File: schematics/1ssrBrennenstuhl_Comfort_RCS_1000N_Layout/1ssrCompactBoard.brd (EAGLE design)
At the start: 46 x 47 mm, 20 parts, among them K1 AQG12105

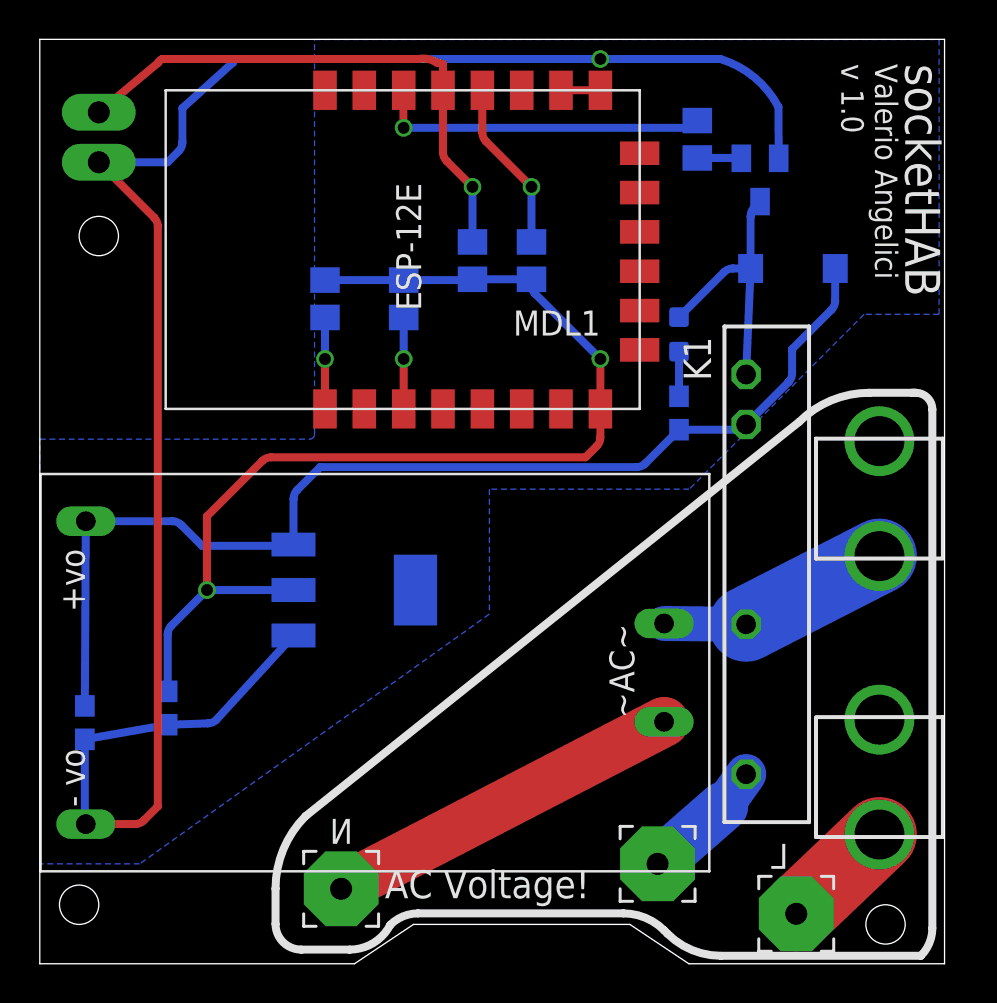
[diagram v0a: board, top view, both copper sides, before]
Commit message: diode moved
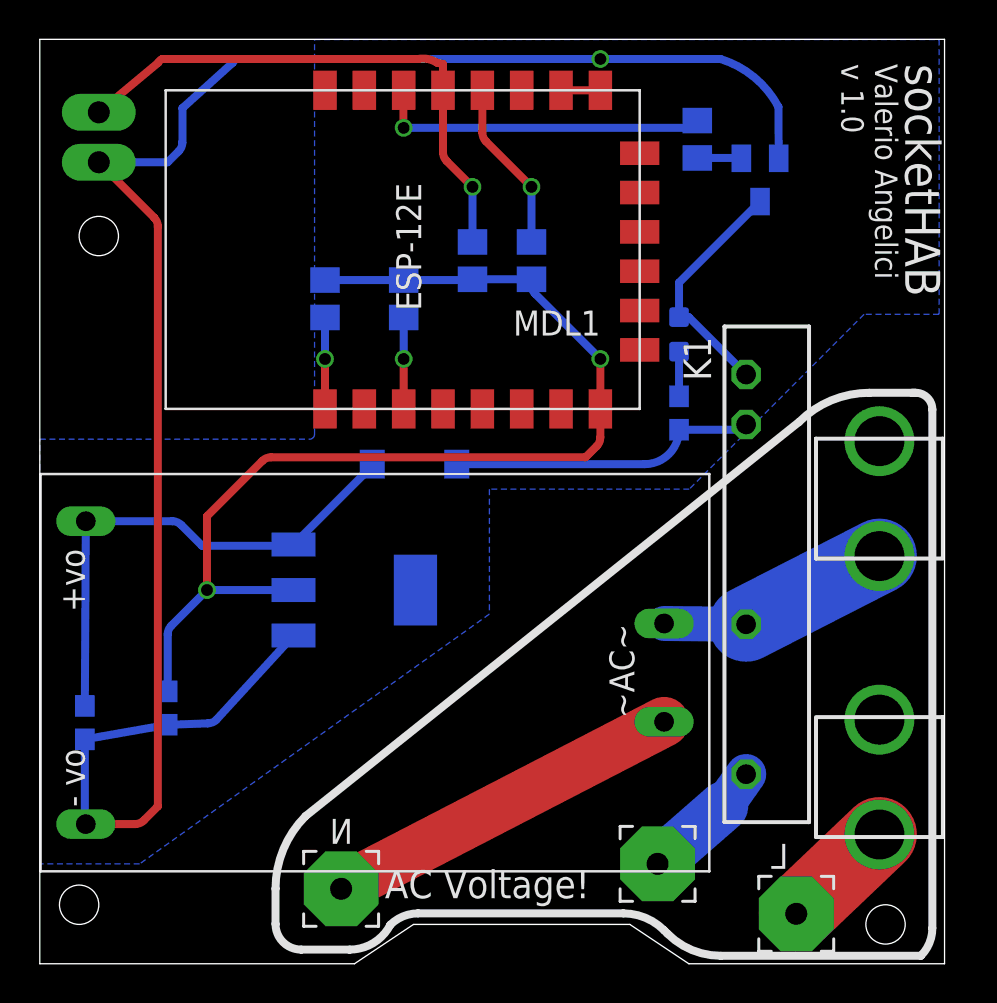
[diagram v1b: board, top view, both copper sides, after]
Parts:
- removed D1: (no value), SparkFun-DiscreteSemi:SMA-DIODE
- added D3: (no value), SparkFun-DiscreteSemi:SMA-DIODE
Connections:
- new net N$3: D3.C, K1.+, R4.2
- net 5V: now also D3.A; no longer D1.C, K1.+, R4.2
- net N$10: no longer D1.A
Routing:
- net 5V: track 57.1 -> 26.3 mm
- net N$3: track 0.00 -> 15.7 mm
- net N$10: track 13.6 -> 12.2 mm
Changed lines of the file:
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@@
 <setting verticaltext="up"/>
 </settings>
-<grid distance="0.05" unitdist="inch" unit="inch" style="lines" multiple="1" display="yes" altdistance="0.025" altunitdist="inch" altunit="inch"/>
+<grid distance="0.05" unitdist="inch" unit="mm" style="lines" multiple="1" display="yes" altdistance="0.025" altunitdist="inch" altunit="mm"/>
 <layers>
 <layer number="1" name="Top" color="4" fill="1" visible="yes" active="yes"/>
@@
 <text x="40.75" y="45.75" size="1.143" layer="112" rot="SR270">Valerio Angelici
 v 1.0</text>
-<text x="6.25" y="8" size="1.016" layer="122" distance="56" rot="MR180">https://github.com/valerioangelici/socketHAB</text>
+<text x="4.98" y="44.83" size="1.016" layer="122" distance="56" rot="MR180">https://github.com/valerioangelici/socketHAB</text>
 <text x="40.75" y="30.5" size="1.143" layer="122" rot="SMR90">Valerio Angelici
 v 1.0</text>
-<text x="23.25" y="9.75" size="1.016" layer="122" rot="SMR0">Fits a Brennstuhl
+<text x="19.44" y="37.69" size="1.016" layer="122" rot="SMR0">Fits a Brennstuhl
 Comfort RCS 1000N</text>
 <wire x1="44.483065625" y1="29.02995" x2="42.183034375" y2="29.02995" width="0.4064" layer="112"/>
@@
 <attribute name="PROD_ID" value="CAP-08604" x="6.5" y="13" size="1.778" layer="28" rot="MR270" display="off"/>
 </element>
-<element name="D1" library="SparkFun-DiscreteSemi" package="SMA-DIODE" value="" x="38.29" y="35.35" rot="MR180"/>
 <element name="K1" library="relay" package="AQG" value="AQG12105" x="35.91" y="19.8" rot="R270">
 <attribute name="MF" value="AROMAT/ MATSUSHITA" x="35.91" y="19.8" size="1.778" layer="27" rot="R270" display="off"/>
@@
 </element>
 <element name="J1" library="SparkFun-Connectors" package="1X02_LONGPADS" value="" x="3" y="40.75" rot="R90"/>
+<element name="D3" library="SparkFun-DiscreteSemi" package="SMA-DIODE" value="" x="19.05" y="25.4" rot="MR180"/>
 </elements>
 <signals>
@@
 <contactref element="U2" pad="3"/>
 <contactref element="C1" pad="1"/>
-<contactref element="K1" pad="+"/>
-<contactref element="D1" pad="C"/>
-<contactref element="R4" pad="2"/>
-<wire x1="32.5" y1="27.15" x2="35.376975" y2="27.15" width="0.4064" layer="16"/>
-<wire x1="35.376975" y1="27.15" x2="35.8259875" y2="27.3359875" width="0.4064" layer="16" curve="45"/>
-<wire x1="35.8259875" y1="27.3359875" x2="35.91" y2="27.42" width="0.4064" layer="16"/>
-<wire x1="40.44" y1="35.35" x2="40.44" y2="33.703025" width="0.4064" layer="16"/>
-<wire x1="40.44" y1="33.703025" x2="40.2540125" y2="33.2540125" width="0.4064" layer="16" curve="-45"/>
-<wire x1="40.2540125" y1="33.2540125" x2="38.25" y2="31.25" width="0.4064" layer="16"/>
-<wire x1="38.25" y1="31.25" x2="38.25" y2="30.023025" width="0.4064" layer="16"/>
-<wire x1="38.25" y1="30.023025" x2="38.0640125" y2="29.5740125" width="0.4064" layer="16" curve="-45"/>
-<wire x1="38.0640125" y1="29.5740125" x2="35.91" y2="27.42" width="0.4064" layer="16"/>
 <wire x1="2.34" y1="22.5" x2="6.736975" y2="22.5" width="0.4064" layer="16"/>
 <wire x1="6.736975" y1="22.5" x2="7.1859875" y2="22.3140125" width="0.4064" layer="16" curve="-45"/>
@@
 <wire x1="8.25" y1="21.25" x2="12.75296875" y2="21.25" width="0.4064" layer="16"/>
 <wire x1="12.75296875" y1="21.25" x2="12.9012" y2="21.3114" width="0.4064" layer="16" curve="45"/>
-<wire x1="12.9012" y1="21.3114" x2="12.9012" y2="23.638175" width="0.4064" layer="16"/>
-<wire x1="12.9012" y1="23.638175" x2="13.0871875" y2="24.0871875" width="0.4064" layer="16" curve="-45"/>
-<wire x1="13.0871875" y1="24.0871875" x2="14.25" y2="25.25" width="0.4064" layer="16"/>
-<wire x1="14.25" y1="25.25" x2="30.336975" y2="25.25" width="0.4064" layer="16"/>
-<wire x1="30.336975" y1="25.25" x2="30.7859875" y2="25.4359875" width="0.4064" layer="16" curve="45"/>
-<wire x1="30.7859875" y1="25.4359875" x2="32.5" y2="27.15" width="0.4064" layer="16"/>
 <wire x1="2.34" y1="22.5" x2="2.29" y2="13.11" width="0.4064" layer="16"/>
+<contactref element="D3" pad="A"/>
+<wire x1="12.9012" y1="21.3114" x2="16.9898" y2="25.4" width="0.4064" layer="16"/>
+<wire x1="16.9898" y1="25.4" x2="16.9" y2="25.4" width="0.4064" layer="16"/>
 </signal>
 <signal name="GPIO0">
@@
 <signal name="N$10">
 <contactref element="K1" pad="-"/>
-<contactref element="D1" pad="A"/>
 <contactref element="Q1" pad="3"/>
 <contactref element="D2" pad="C"/>
-<wire x1="35.91" y1="29.96" x2="36.14" y2="35.35" width="0.4064" layer="16"/>
-<wire x1="36.62" y1="38.75" x2="36.3259875" y2="38.4559875" width="0.4064" layer="16"/>
-<wire x1="36.3259875" y1="38.4559875" x2="36.14" y2="38.006975" width="0.4064" layer="16" curve="45"/>
-<wire x1="36.14" y1="38.006975" x2="36.14" y2="35.35" width="0.4064" layer="16"/>
-<wire x1="32.5" y1="32.877" x2="34.7870125" y2="35.1640125" width="0.4064" layer="16"/>
-<wire x1="34.7870125" y1="35.1640125" x2="35.236025" y2="35.35" width="0.4064" layer="16" curve="-45"/>
-<wire x1="35.236025" y1="35.35" x2="36.14" y2="35.35" width="0.4064" layer="16"/>
+<wire x1="32.5" y1="32.877" x2="32.993" y2="32.877" width="0.4064" layer="16"/>
+<wire x1="32.993" y1="32.877" x2="35.91" y2="29.96" width="0.4064" layer="16"/>
+<wire x1="36.62" y1="38.75" x2="32.5" y2="34.63" width="0.4064" layer="16"/>
+<wire x1="32.5" y1="34.63" x2="32.5" y2="32.877" width="0.4064" layer="16"/>
 </signal>
 <signal name="N$12">
@@
 <signal name="N$2">
 </signal>
+<signal name="N$3">
+<contactref element="K1" pad="+"/>
+<contactref element="R4" pad="2"/>
+<wire x1="32.5" y1="27.15" x2="35.91" y2="27.15" width="0.4064" layer="16"/>
+<wire x1="35.91" y1="27.15" x2="35.91" y2="27.42" width="0.4064" layer="16"/>
+<contactref element="D3" pad="C"/>
+<wire x1="32.5" y1="27.15" x2="30.75" y2="25.4" width="0.4064" layer="16" curve="-90"/>
+<wire x1="30.75" y1="25.4" x2="21.2" y2="25.4" width="0.4064" layer="16"/>
+</signal>
 </signals>
